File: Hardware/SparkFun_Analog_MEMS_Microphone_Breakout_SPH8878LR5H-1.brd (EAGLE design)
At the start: 14 x 10.2 mm, 25 parts, among them U1 OPA344, U3 SPH8878LR5H-1

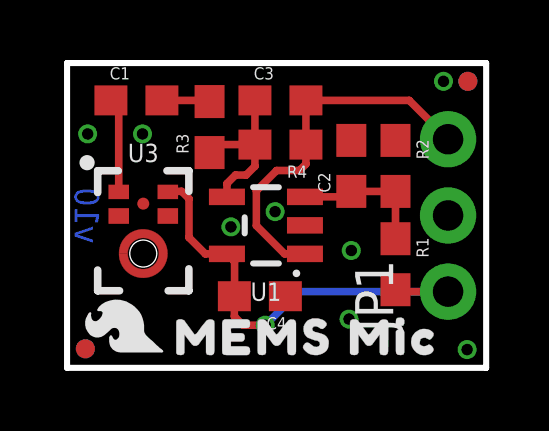
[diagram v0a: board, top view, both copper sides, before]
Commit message: Added test point for OUT-
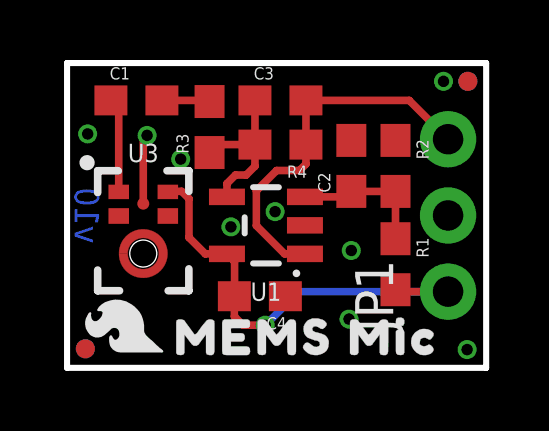
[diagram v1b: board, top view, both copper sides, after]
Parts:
- added OUT-: (no value), SparkFun-Connectors:TP_15TH
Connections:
- new net N$3: OUT-.1, U3.6
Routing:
- net N$3: track 0.00 -> 2.33 mm
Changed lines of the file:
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@@
 <setting verticaltext="up"/>
 </settings>
-<grid distance="0.05" unitdist="inch" unit="inch" style="lines" multiple="1" display="yes" altdistance="0.005" altunitdist="inch" altunit="inch"/>
+<grid distance="0.05" unitdist="inch" unit="inch" style="lines" multiple="1" display="yes" altdistance="0.0001" altunitdist="inch" altunit="inch"/>
 <layers>
 <layer number="1" name="Top" color="4" fill="1" visible="yes" active="yes"/>
@@
 <layer number="56" name="wert" color="7" fill="1" visible="no" active="yes"/>
 <layer number="57" name="tCAD" color="7" fill="1" visible="no" active="no"/>
+<layer number="58" name="bCAD" color="7" fill="1" visible="no" active="no"/>
 <layer number="59" name="tCarbon" color="7" fill="1" visible="no" active="no"/>
 <layer number="60" name="bCarbon" color="7" fill="1" visible="no" active="no"/>
@@
 <layer number="98" name="Guide" color="6" fill="1" visible="no" active="no"/>
 <layer number="99" name="SpiceOrder" color="7" fill="1" visible="no" active="no"/>
-<layer number="100" name="Muster" color="7" fill="1" visible="yes" active="yes"/>
+<layer number="100" name="Muster" color="7" fill="1" visible="no" active="yes"/>
 <layer number="101" name="Patch_Top" color="12" fill="4" visible="no" active="yes"/>
 <layer number="102" name="Vscore" color="7" fill="1" visible="no" active="yes"/>
@@
 <layer number="250" name="Descript" color="3" fill="1" visible="no" active="no"/>
 <layer number="251" name="SMDround" color="12" fill="11" visible="no" active="no"/>
+<layer number="253" name="Extra" color="7" fill="1" visible="no" active="no"/>
 <layer number="254" name="cooling" color="7" fill="1" visible="no" active="yes"/>
 <layer number="255" name="routoute" color="7" fill="1" visible="no" active="no"/>
@@
 <element name="U$7" library="output" package="MEMS_MIC0" value="" x="8.001" y="1.016" smashed="yes"/>
 <element name="U$9" library="output" package="SPH8878LR5H#10" value="" x="6.731" y="0.889" smashed="yes" rot="MR0"/>
+<element name="OUT-" library="SparkFun-Connectors" package="TP_15TH" value="" x="2.667" y="7.747" smashed="yes" rot="MR0"/>
 </elements>
 <signals>
@@
 <via x="13.335" y="0.6096" extent="1-16" drill="0.381"/>
 <via x="9.398" y="1.6256" extent="1-16" drill="0.381"/>
-<via x="2.5146" y="7.7978" extent="1-16" drill="0.381"/>
+<via x="3.787140625" y="6.957059375" extent="1-16" drill="0.381"/>
 <via x="9.4742" y="3.9116" extent="1-16" drill="0.381"/>
 <via x="5.461" y="4.699" extent="1-16" drill="0.381"/>
@@
 <wire x1="7.747" y1="6.5786" x2="7.962" y2="6.7936" width="0.254" layer="1"/>
 </signal>
+<signal name="N$3">
+<contactref element="U3" pad="6"/>
+<contactref element="OUT-" pad="1"/>
+<wire x1="2.54" y1="5.473" x2="2.54" y2="7.62" width="0.254" layer="1"/>
+<wire x1="2.54" y1="7.62" x2="2.667" y2="7.747" width="0.254" layer="1"/>
+</signal>
 </signals>

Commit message: Checklist catches
-Attribution for original design
-test point for OUT- moved to 50 though grid
-nudges some vias to avoid silk
-adjust value text objects for assembly sheet
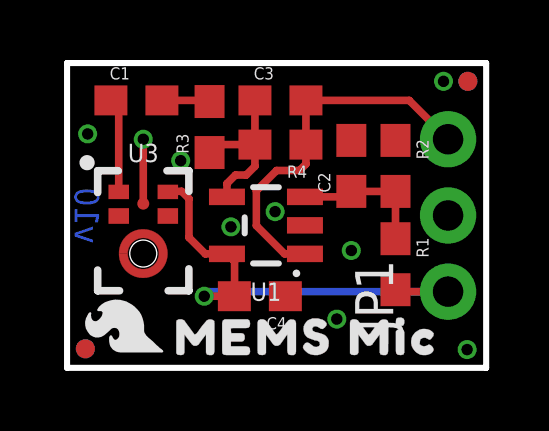
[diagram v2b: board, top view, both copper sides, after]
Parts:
- moved OUT- 0.18 mm to (2.54, 7.62)
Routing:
- net VCC: track 15.3 -> 16.1 mm
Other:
- board text added: "Based on a MEMs mic design by Pete Dokter"
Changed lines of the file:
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@@
 <setting verticaltext="up"/>
 </settings>
-<grid distance="0.05" unitdist="inch" unit="inch" style="lines" multiple="1" display="yes" altdistance="0.0001" altunitdist="inch" altunit="inch"/>
+<grid distance="0.05" unitdist="inch" unit="inch" style="lines" multiple="1" display="yes" altdistance="0.001" altunitdist="inch" altunit="inch"/>
 <layers>
 <layer number="1" name="Top" color="4" fill="1" visible="yes" active="yes"/>
@@
 <dimension x1="0" y1="0" x2="2.54" y2="3.81" x3="-3.81" y3="1.905" textsize="1.27" textratio="15" layer="47" dtype="vertical" width="0.0762" unit="inch"/>
 <text x="-2.54" y="22.86" size="1.27" layer="47" font="vector">Units: INCHES</text>
+<text x="-7.62" y="-13.97" size="1.778" layer="51" font="vector" ratio="9">Based on a MEMs mic design by Pete Dokter</text>
 </plain>
 <attributes>
@@
 <attribute name="NAME" x="7.3152" y="1.6891" size="0.4064" layer="25" rot="R180"/>
 <attribute name="PROD_ID" value="CAP-00810" x="6.4262" y="2.3876" size="1.778" layer="27" rot="R180" display="off"/>
-<attribute name="VALUE" value="0.1uF" x="7.3025" y="1.8034" size="0.4064" layer="27" font="vector" ratio="12" rot="R180"/>
+<attribute name="VALUE" value="0.1uF" x="9.6139" y="2.5908" size="0.4064" layer="27" font="vector" ratio="12" rot="R180"/>
 </element>
 <element name="C1" library="SparkFun-Capacitors" package="0603" value="4.7uF" x="2.3114" y="8.9154" smashed="yes">
@@
 <attribute name="VALUE" x="6.4262" y="4.8514" size="0.4064" layer="27" font="vector" ratio="12" rot="R270" align="bottom-center"/>
 </element>
-<element name="LOGO1" library="SparkFun-Aesthetics" package="SFE_LOGO_FLAME_.1" value="SFE_LOGO_FLAME.1_INCH" x="2.5146" y="6.5532" smashed="yes" rot="MR270"/>
+<element name="LOGO1" library="SparkFun-Aesthetics" package="SFE_LOGO_FLAME_.1" value="SFE_LOGO_FLAME.1_INCH" x="2.5146" y="6.5278" smashed="yes" rot="MR270"/>
 <element name="LOGO2" library="SparkFun-Aesthetics" package="OSHW-LOGO-MINI" value="OSHW-LOGOMINI" x="2.54" y="3.81" smashed="yes" rot="MR270"/>
 <element name="FRAME2" library="SparkFun-Aesthetics" package="CREATIVE_COMMONS" value="FRAME-LETTER" x="-19.05" y="-11.43" smashed="yes">
@@
 <attribute name="NAME" x="2.54" y="6.858" size="0.6096" layer="25" font="vector" ratio="20" align="bottom-center"/>
 <attribute name="PROD_ID" value="IC-16576" x="2.54" y="3.81" size="1.778" layer="27" font="vector" ratio="15" display="off"/>
-<attribute name="VALUE" x="2.54" y="2.032" size="0.6096" layer="27" font="vector" ratio="20" align="top-center"/>
+<attribute name="VALUE" x="0.254" y="5.0292" size="0.6096" layer="27" font="vector" ratio="20" rot="R90" align="top-center"/>
 </element>
 <element name="U$7" library="output" package="MEMS_MIC0" value="" x="8.001" y="1.016" smashed="yes"/>
 <element name="U$9" library="output" package="SPH8878LR5H#10" value="" x="6.731" y="0.889" smashed="yes" rot="MR0"/>
-<element name="OUT-" library="SparkFun-Connectors" package="TP_15TH" value="" x="2.667" y="7.747" smashed="yes" rot="MR0"/>
+<element name="OUT-" library="SparkFun-Connectors" package="TP_15TH" value="" x="2.54" y="7.62" smashed="yes" rot="MR0"/>
 </elements>
 <signals>
 <signal name="N$1">
 <contactref element="C1" pad="1"/>
-<wire x1="1.702" y1="8.6748" x2="1.4614" y2="8.9154" width="0.254" layer="1"/>
 <contactref element="U3" pad="1"/>
 <wire x1="1.4614" y1="8.9154" x2="1.722" y2="8.6548" width="0.254" layer="1"/>
@@
 <via x="12.5476" y="9.5504" extent="1-16" drill="0.381"/>
 <via x="13.335" y="0.6096" extent="1-16" drill="0.381"/>
-<via x="9.398" y="1.6256" extent="1-16" drill="0.381"/>
-<via x="3.787140625" y="6.957059375" extent="1-16" drill="0.381"/>
+<via x="8.9916" y="1.6256" extent="1-16" drill="0.381"/>
+<via x="3.787140625" y="6.906259375" extent="1-16" drill="0.381"/>
 <via x="9.4742" y="3.9116" extent="1-16" drill="0.381"/>
 <via x="5.461" y="4.699" extent="1-16" drill="0.381"/>
@@
 <wire x1="5.5762" y1="2.3876" x2="5.5833" y2="2.3947" width="0.254" layer="1"/>
 <wire x1="5.5833" y1="3.5458" x2="5.3293" y2="3.7998" width="0.254" layer="1"/>
-<wire x1="6.604" y1="1.4224" x2="5.8674" y2="1.4224" width="0.254" layer="1"/>
-<wire x1="5.5762" y1="2.3876" x2="5.5762" y2="1.7136" width="0.254" layer="1"/>
-<wire x1="5.8674" y1="1.4224" x2="5.5762" y2="1.7136" width="0.254" layer="1"/>
-<via x="6.604" y="1.4224" extent="1-16" drill="0.381"/>
-<wire x1="6.604" y1="1.4224" x2="7.7216" y2="2.54" width="0.254" layer="16"/>
-<wire x1="7.7216" y1="2.54" x2="12.7" y2="2.54" width="0.254" layer="16"/>
+<wire x1="4.572" y1="2.3876" x2="5.5762" y2="2.3876" width="0.254" layer="1"/>
+<via x="4.572" y="2.3876" extent="1-16" drill="0.381"/>
+<wire x1="4.572" y1="2.3876" x2="4.7244" y2="2.54" width="0.254" layer="16"/>
+<wire x1="4.7244" y1="2.54" x2="12.7" y2="2.54" width="0.254" layer="16"/>
 <wire x1="10.9474" y1="2.6044" x2="11.0118" y2="2.54" width="0.254" layer="1"/>
 <wire x1="11.0118" y1="2.54" x2="12.7" y2="2.54" width="0.254" layer="1"/>
@@
 <contactref element="OUT-" pad="1"/>
 <wire x1="2.54" y1="5.473" x2="2.54" y2="7.62" width="0.254" layer="1"/>
-<wire x1="2.54" y1="7.62" x2="2.667" y2="7.747" width="0.254" layer="1"/>
 </signal>
 </signals>
 <mfgpreviewcolors>
-<mfgpreviewcolor name="soldermaskcolor" color="0xC8008000"/>
+<mfgpreviewcolor name="soldermaskcolor" color="0xC8AA0000"/>
 <mfgpreviewcolor name="silkscreencolor" color="0xFFFEFEFE"/>
 <mfgpreviewcolor name="backgroundcolor" color="0xFF282828"/>
